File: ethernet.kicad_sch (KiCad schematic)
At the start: 27 parts, among them J6 RJ45_RB1-125B8G1A, U6 RTL8111H-CG-RH, U7 D3V3XA4B10LP, U79 D3V3XA4B10LP, Y1 25MHz

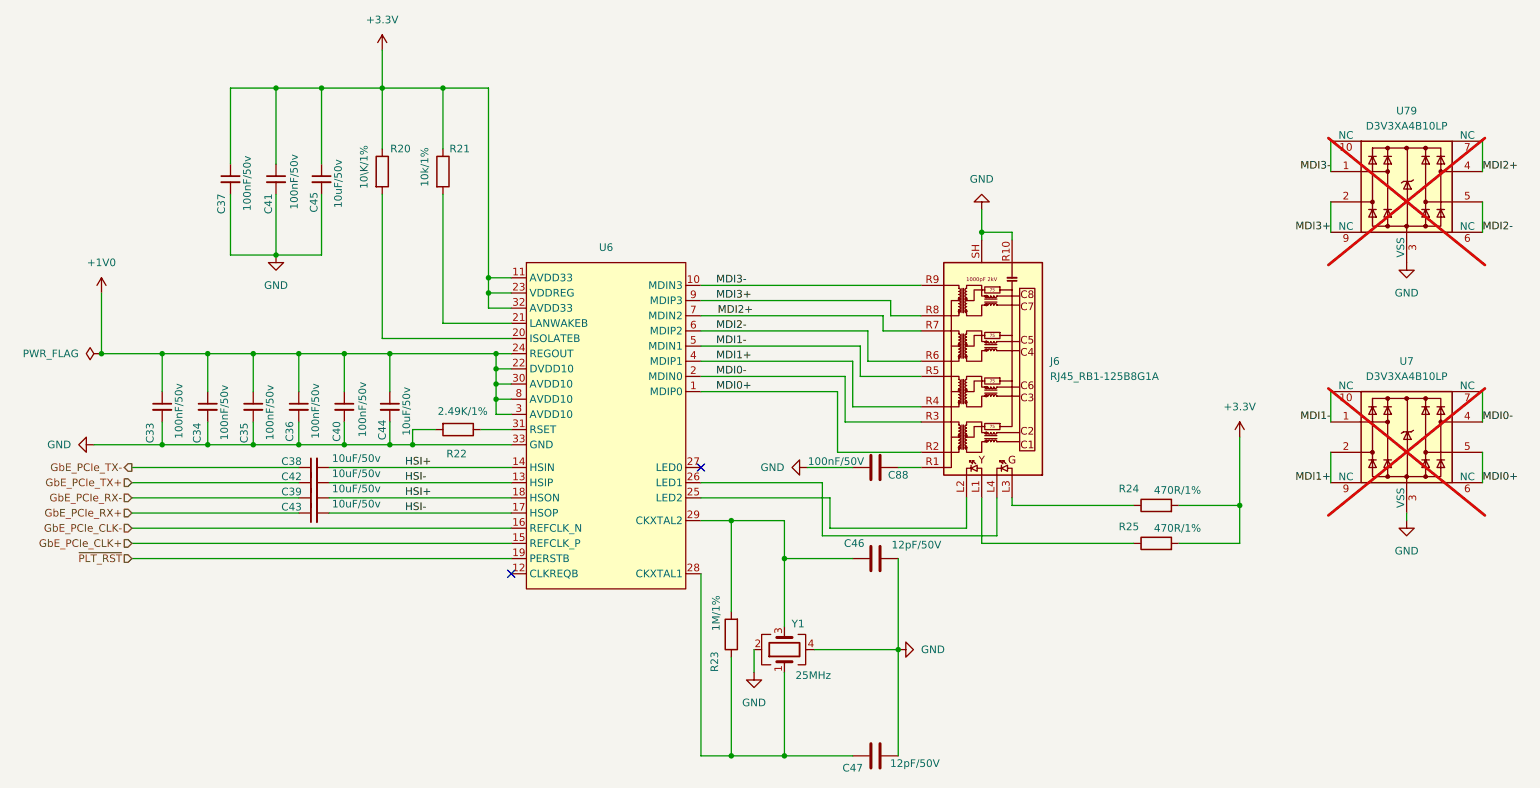
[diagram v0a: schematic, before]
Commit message: Updated all the footprints into the pcb editor but all the designator numbers have changed... I have tp go back and fix each one
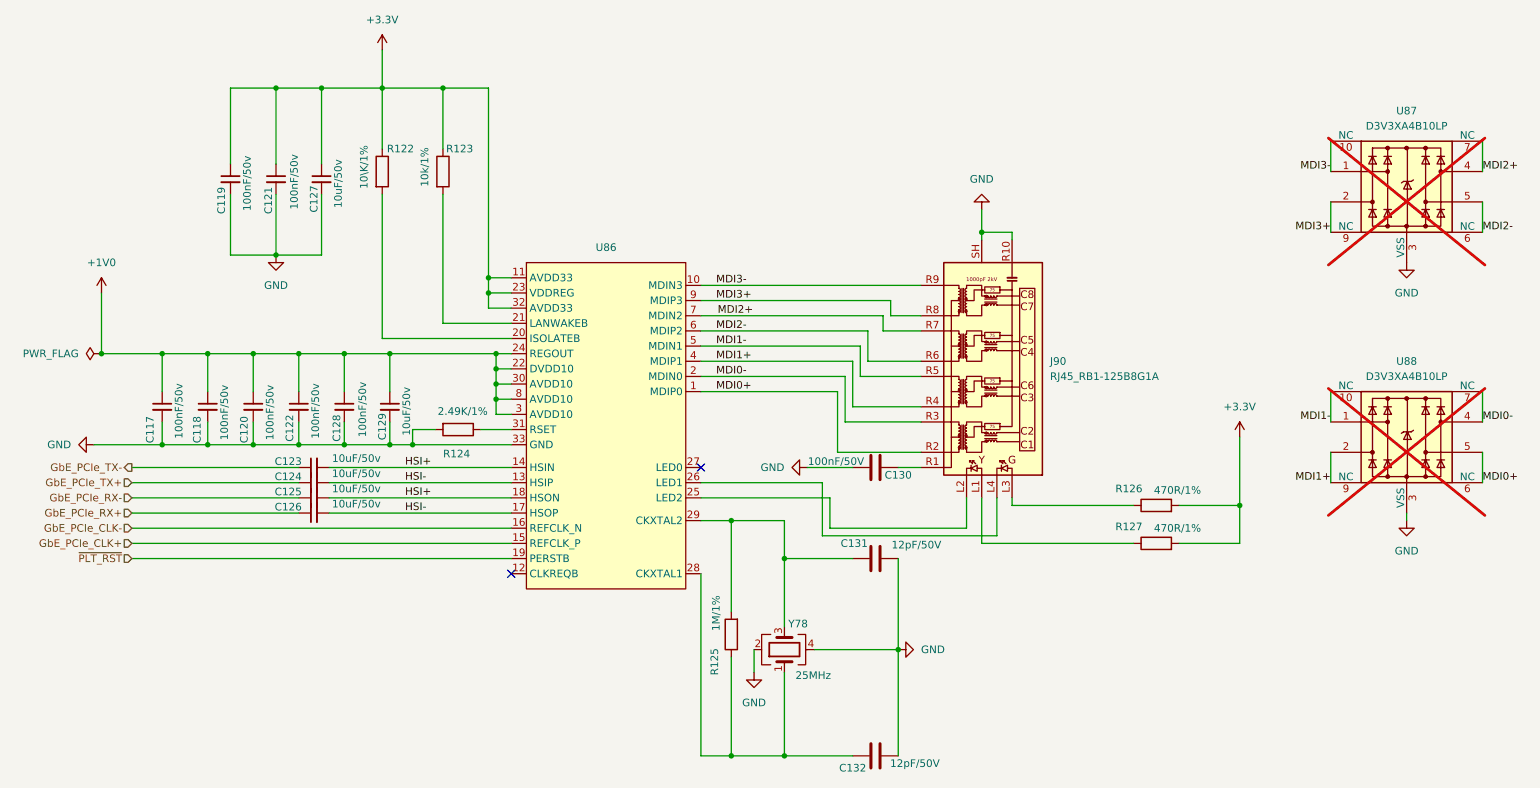
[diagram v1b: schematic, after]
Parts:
- C131: renamed from C46; footprint (none) -> A_HDJ_Library:C_0402_1005Metric
- C132: renamed from C47; footprint (none) -> A_HDJ_Library:C_0402_1005Metric
- Y78: renamed from Y1; footprint (none) -> A_HDJ_Library:Crystal_SMD_3225-4Pin_3.2x2.5mm
- renumbered C33 to C117, C34 to C118, C37 to C119, C35 to C120, C41 to C121, C36 to C122, C38 to C123, C42 to C124, C39 to C125, C43 to C126, C45 to C127, C40 to C128, C44 to C129, C88 to C130, J6 to J90, R20 to R122, R21 to R123, R22 to R124, R23 to R125, R24 to R126, R25 to R127, U6 to U86, U79 to U87, U7 to U88

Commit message: Designators in ethernet restored
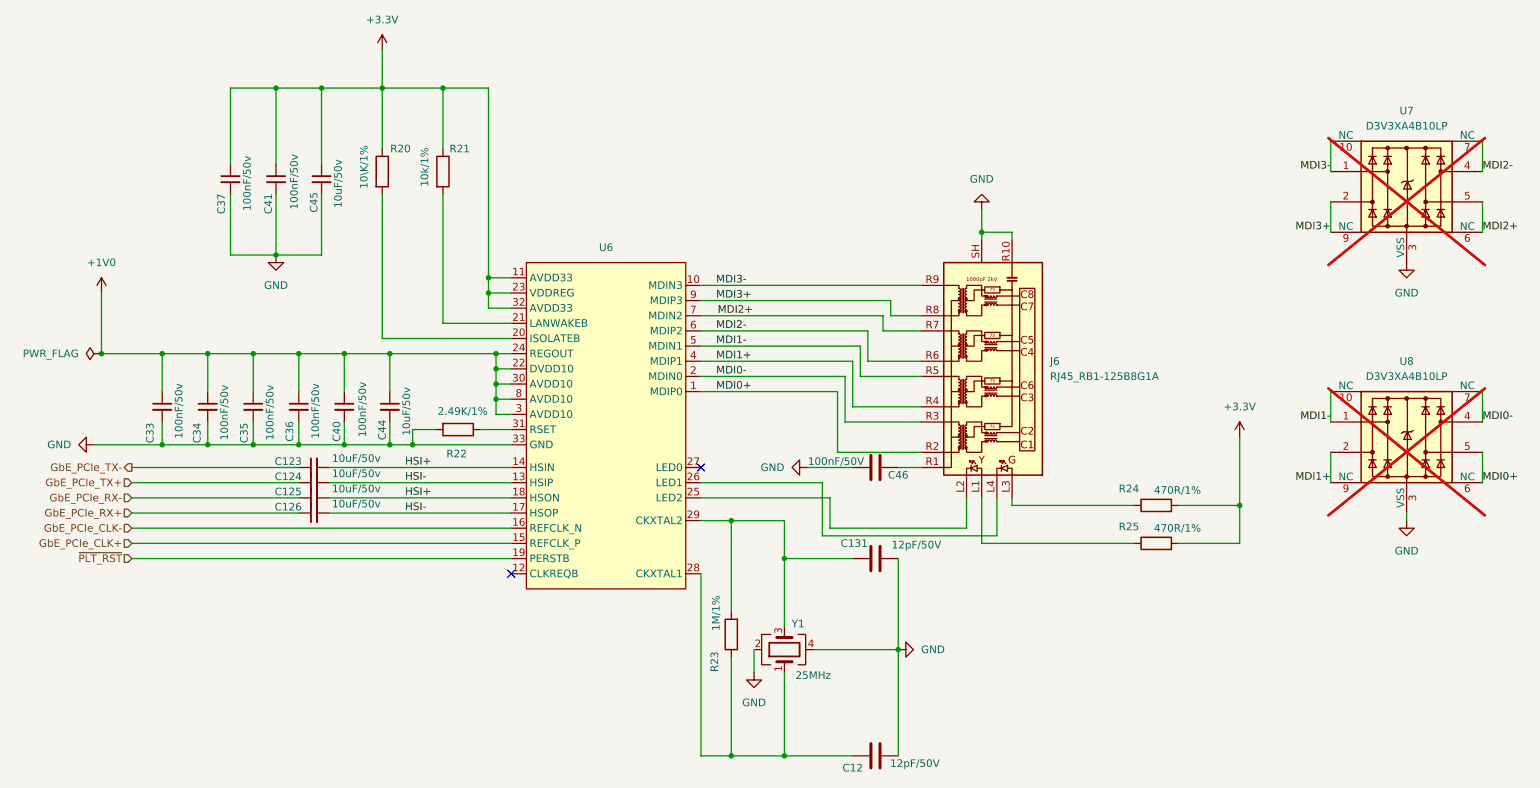
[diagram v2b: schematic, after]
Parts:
- renumbered C132 to C12, C117 to C33, C118 to C34, C120 to C35, C122 to C36, C119 to C37, C128 to C40, C121 to C41, C129 to C44, C127 to C45, C130 to C46, J90 to J6, R122 to R20, R123 to R21, R124 to R22, R125 to R23, R126 to R24, R127 to R25, U86 to U6, U87 to U7, U88 to U8, Y78 to Y1
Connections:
- net MDI2+: now also U7.5, U7.6 (NC); no longer U7.4, U7.7 (NC)
- net MDI2-: now also U7.4, U7.7 (NC); no longer U7.5, U7.6 (NC)
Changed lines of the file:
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@@
 		)
 	)
-	(label "MDI3+"
-		(at 128.27 66.04 0)
+	(label "MDI2+"
+		(at 256.54 54.61 0)
 		(effects
 			(font
@@
 	)
 	(label "MDI3+"
-		(at 231.14 54.61 180)
+		(at 128.27 66.04 0)
 		(effects
 			(font
 				(size 1.27 1.27)
 			)
-			(justify right bottom)
+			(justify left bottom)
 		)
 	)
-	(label "MDI0-"
-		(at 128.27 78.74 0)
+	(label "MDI3+"
+		(at 231.14 54.61 180)
 		(effects
 			(font
 				(size 1.27 1.27)
 			)
-			(justify left bottom)
+			(justify right bottom)
 		)
 	)
-	(label "MDI2-"
-		(at 256.54 54.61 0)
+	(label "MDI0-"
+		(at 128.27 78.74 0)
 		(effects
 			(font
@@
 		)
 	)
-	(label "MDI3-"
-		(at 128.27 63.5 0)
+	(label "MDI2-"
+		(at 256.54 44.45 0)
 		(effects
 			(font
@@
 		)
 	)
-	(label "MDI2+"
-		(at 256.54 44.45 0)
+	(label "MDI3-"
+		(at 128.27 63.5 0)
 		(effects
 			(font
@@
 		(in_pos_files yes)
 		(dnp no)
-		(property "Reference" "C119"
+		(property "Reference" "C37"
 			(at 45.466 51.562 90)
 			(show_name no)
@@
 			(project "Carrier_Board"
 				(path "/e768274e-12f3-4f83-96f6-abb7638e0bc1/3ad1df68-0a03-497a-a7ee-c67c9856d4e6"
-					(reference "C119")
+					(reference "C37")
 					(unit 1)
 				)
@@
 		(in_pos_files yes)
 		(dnp no)
-		(property "Reference" "C129"
+		(property "Reference" "C44"
 			(at 72.39 89.408 90)
 			(show_name no)
@@
 			(project "Carrier_Board"
 				(path "/e768274e-12f3-4f83-96f6-abb7638e0bc1/3ad1df68-0a03-497a-a7ee-c67c9856d4e6"
-					(reference "C129")
+					(reference "C44")
 					(unit 1)
 				)
@@
 		(in_pos_files yes)
 		(dnp no)
-		(property "Reference" "R124"
+		(property "Reference" "R22"
 			(at 84.836 91.694 90)
 			(show_name no)
@@
 			(project "Carrier_Board"
 				(path "/e768274e-12f3-4f83-96f6-abb7638e0bc1/3ad1df68-0a03-497a-a7ee-c67c9856d4e6"
-					(reference "R124")
+					(reference "R22")
 					(unit 1)
 				)
@@
 		(dnp no)
 		(fields_autoplaced yes)
-		(property "Reference" "U86"
+		(property "Reference" "U6"
 			(at 109.855 57.15 0)
 			(show_name no)
@@
 			(project "Carrier_Board"
 				(path "/e768274e-12f3-4f83-96f6-abb7638e0bc1/3ad1df68-0a03-497a-a7ee-c67c9856d4e6"
-					(reference "U86")
+					(reference "U6")
 					(unit 1)
 				)
@@
 		(in_pos_files yes)
 		(dnp no)
-		(property "Reference" "R127"
+		(property "Reference" "R25"
 			(at 197.358 103.886 90)
 			(show_name no)
@@
 			(project "Carrier_Board"
 				(path "/e768274e-12f3-4f83-96f6-abb7638e0bc1/3ad1df68-0a03-497a-a7ee-c67c9856d4e6"
-					(reference "R127")
+					(reference "R25")
 					(unit 1)
 				)
@@
 		(in_pos_files yes)
 		(dnp no)
-		(property "Reference" "R126"
+		(property "Reference" "R24"
 			(at 197.358 97.536 90)
 			(show_name no)
@@
 			(project "Carrier_Board"
 				(path "/e768274e-12f3-4f83-96f6-abb7638e0bc1/3ad1df68-0a03-497a-a7ee-c67c9856d4e6"
-					(reference "R126")
+					(reference "R24")
 					(unit 1)
 				)
@@
 		(in_pos_files yes)
 		(dnp no)
-		(property "Reference" "C121"
+		(property "Reference" "C41"
 			(at 53.34 51.562 90)
 			(show_name no)
@@
 			(project "Carrier_Board"
 				(path "/e768274e-12f3-4f83-96f6-abb7638e0bc1/3ad1df68-0a03-497a-a7ee-c67c9856d4e6"
-					(reference "C121")
+					(reference "C41")
 					(unit 1)
 				)
@@
 		(dnp yes)
 		(fields_autoplaced yes)
-		(property "Reference" "U88"
+		(property "Reference" "U8"
 			(at 243.84 76.2 0)
 			(show_name no)
@@
 			(project "Carrier_Board"
 				(path "/e768274e-12f3-4f83-96f6-abb7638e0bc1/3ad1df68-0a03-497a-a7ee-c67c9856d4e6"
-					(reference "U88")
+					(reference "U8")
 					(unit 1)
 				)
@@
 		(in_pos_files yes)
 		(dnp no)
-		(property "Reference" "R122"
+		(property "Reference" "R20"
 			(at 75.438 40.64 0)
 			(show_name no)
@@
 			(project "Carrier_Board"
 				(path "/e768274e-12f3-4f83-96f6-abb7638e0bc1/3ad1df68-0a03-497a-a7ee-c67c9856d4e6"
-					(reference "R122")
+					(reference "R20")
 					(unit 1)
 				)
@@
 		(in_pos_files yes)
 		(dnp no)
-		(property "Reference" "C127"
+		(property "Reference" "C45"
 			(at 60.96 51.308 90)
 			(show_name no)
@@
 			(project "Carrier_Board"
 				(path "/e768274e-12f3-4f83-96f6-abb7638e0bc1/3ad1df68-0a03-497a-a7ee-c67c9856d4e6"
-					(reference "C127")
+					(reference "C45")
 					(unit 1)
 				)
@@
 		(dnp no)
 		(fields_autoplaced yes)
-		(property "Reference" "J90"
+		(property "Reference" "J6"
 			(at 184.15 76.1999 0)
 			(show_name no)
@@
 			(project "Carrier_Board"
 				(path "/e768274e-12f3-4f83-96f6-abb7638e0bc1/3ad1df68-0a03-497a-a7ee-c67c9856d4e6"
-					(reference "J90")
+					(reference "J6")
 					(unit 1)
 				)
@@
 		(in_pos_files yes)
 		(dnp no)
-		(property "Reference" "C132"
+		(property "Reference" "C12"
 			(at 151.13 144.272 90)
 			(show_name no)
@@
 			(project "Carrier_Board"
 				(path "/e768274e-12f3-4f83-96f6-abb7638e0bc1/3ad1df68-0a03-497a-a7ee-c67c9856d4e6"
-					(reference "C132")
+					(reference "C12")
 					(unit 1)
 				)
@@
 		(in_pos_files yes)
 		(dnp no)
-		(property "Reference" "C122"
+		(property "Reference" "C36"
 			(at 56.896 89.662 90)
 			(show_name no)
@@
 			(project "Carrier_Board"
 				(path "/e768274e-12f3-4f83-96f6-abb7638e0bc1/3ad1df68-0a03-497a-a7ee-c67c9856d4e6"
-					(reference "C122")
+					(reference "C36")
 					(unit 1)
 				)
@@
 		(in_pos_files yes)
 		(dnp no)
-		(property "Reference" "Y78"
+		(property "Reference" "Y1"
 			(at 141.986 120.142 90)
 			(show_name no)
@@
 			(project "Carrier_Board"
 				(path "/e768274e-12f3-4f83-96f6-abb7638e0bc1/3ad1df68-0a03-497a-a7ee-c67c9856d4e6"
-					(reference "Y78")
+					(reference "Y1")
 					(unit 1)
 				)
@@
 		(in_pos_files yes)
 		(dnp no)
-		(property "Reference" "C130"
+		(property "Reference" "C46"
 			(at 158.75 95.25 90)
 			(show_name no)
@@
 			(project "Carrier_Board"
 				(path "/e768274e-12f3-4f83-96f6-abb7638e0bc1/3ad1df68-0a03-497a-a7ee-c67c9856d4e6"
-					(reference "C130")
+					(reference "C46")
 					(unit 1)
 				)
@@
 		(in_pos_files yes)
 		(dnp no)
-		(property "Reference" "R125"
+		(property "Reference" "R23"
 			(at 128.016 126.492 90)
 			(show_name no)
@@
 			(project "Carrier_Board"
 				(path "/e768274e-12f3-4f83-96f6-abb7638e0bc1/3ad1df68-0a03-497a-a7ee-c67c9856d4e6"
-					(reference "R125")
+					(reference "R23")
 					(unit 1)
 				)
@@
 		(in_pos_files yes)
 		(dnp no)
-		(property "Reference" "C120"
+		(property "Reference" "C35"
 			(at 49.276 89.916 90)
 			(show_name no)
@@
 			(project "Carrier_Board"
 				(path "/e768274e-12f3-4f83-96f6-abb7638e0bc1/3ad1df68-0a03-497a-a7ee-c67c9856d4e6"
-					(reference "C120")
+					(reference "C35")
 					(unit 1)
 				)
@@
 		(in_pos_files yes)
 		(dnp no)
-		(property "Reference" "C118"
+		(property "Reference" "C34"
 			(at 41.402 89.916 90)
 			(show_name no)
@@
 			(project "Carrier_Board"
 				(path "/e768274e-12f3-4f83-96f6-abb7638e0bc1/3ad1df68-0a03-497a-a7ee-c67c9856d4e6"
-					(reference "C118")
+					(reference "C34")
 					(unit 1)
 				)
@@
 		(in_pos_files yes)
 		(dnp no)
-		(property "Reference" "C117"
+		(property "Reference" "C33"
 			(at 33.528 89.916 90)
 			(show_name no)
@@
 			(project "Carrier_Board"
 				(path "/e768274e-12f3-4f83-96f6-abb7638e0bc1/3ad1df68-0a03-497a-a7ee-c67c9856d4e6"
-					(reference "C117")
+					(reference "C33")
 					(unit 1)
 				)
@@
 		(in_pos_files yes)
 		(dnp no)
-		(property "Reference" "C128"
+		(property "Reference" "C40"
 			(at 64.77 89.662 90)
 			(show_name no)
@@
 			(project "Carrier_Board"
 				(path "/e768274e-12f3-4f83-96f6-abb7638e0bc1/3ad1df68-0a03-497a-a7ee-c67c9856d4e6"
-					(reference "C128")
+					(reference "C40")
 					(unit 1)
 				)
@@
 		(in_pos_files yes)
 		(dnp no)
-		(property "Reference" "R123"
+		(property "Reference" "R21"
 			(at 85.344 40.64 0)
 			(show_name no)
@@
 			(project "Carrier_Board"
 				(path "/e768274e-12f3-4f83-96f6-abb7638e0bc1/3ad1df68-0a03-497a-a7ee-c67c9856d4e6"
-					(reference "R123")
+					(reference "R21")
 					(unit 1)
 				)
@@
 		(dnp yes)
 		(fields_autoplaced yes)
-		(property "Reference" "U87"
+		(property "Reference" "U7"
 			(at 243.84 34.29 0)
 			(show_name no)
@@
 			(project "Carrier_Board"
 				(path "/e768274e-12f3-4f83-96f6-abb7638e0bc1/3ad1df68-0a03-497a-a7ee-c67c9856d4e6"
-					(reference "U87")
+					(reference "U7")
 					(unit 1)
 				)
